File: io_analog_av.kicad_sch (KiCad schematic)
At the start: 15 parts, among them J10 ICD15S13E4GX00LF, J11 PJRAN3X1U03X, J13 SJ1-3533NG, J14 PJRAN2X1U02X, J17 K-SCARTX-022, U20 FSA2275UMX

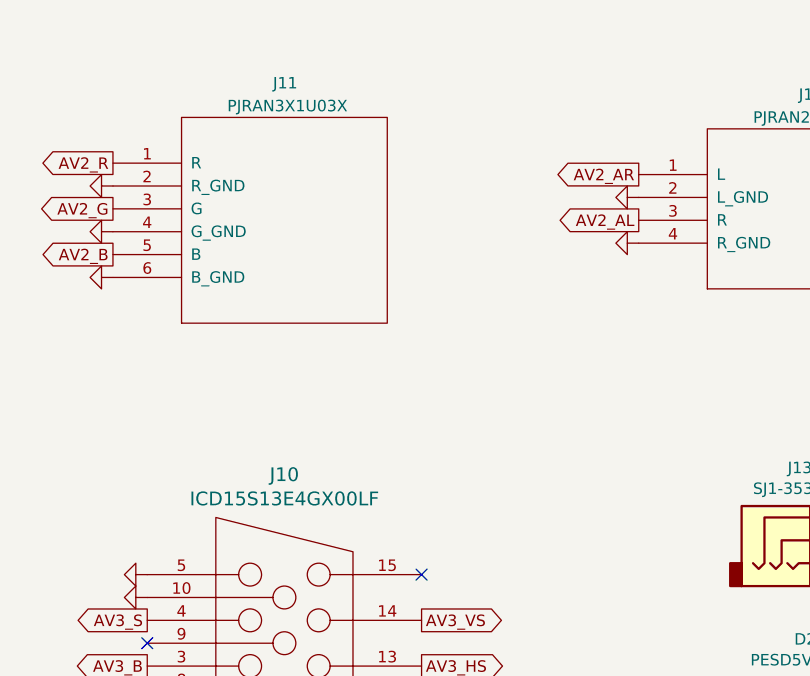
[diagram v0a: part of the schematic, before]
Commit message: update schematic to v1.5
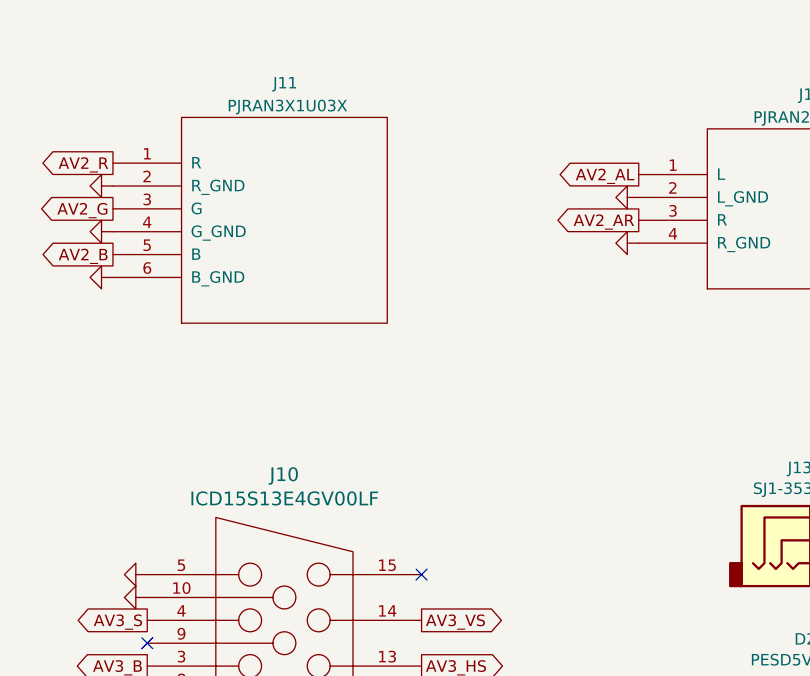
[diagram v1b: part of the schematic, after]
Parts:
- J10: value ICD15S13E4GX00LF -> ICD15S13E4GV00LF
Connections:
- net AV2_AL: now also J14.1 (L); no longer J14.3 (R)
- net AV2_AR: now also J14.3 (R); no longer J14.1 (L)

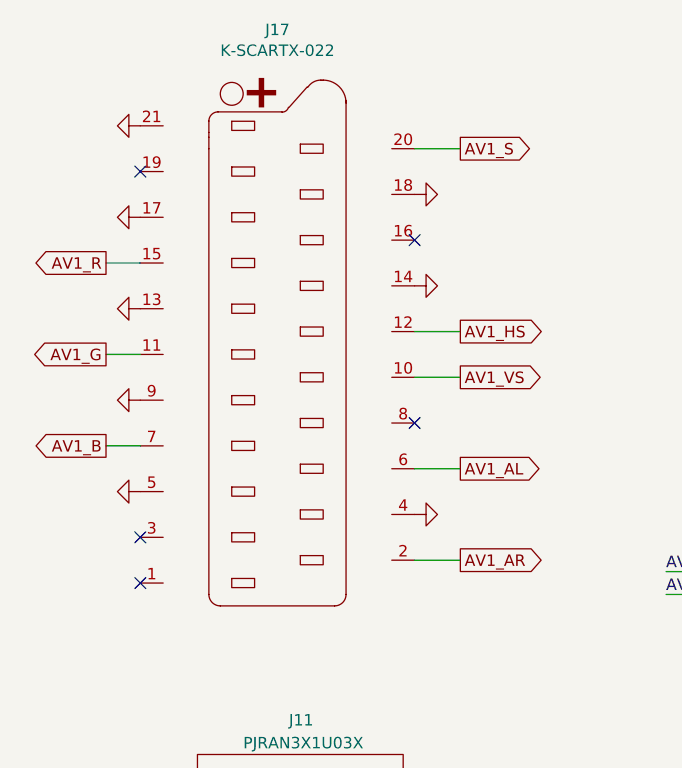
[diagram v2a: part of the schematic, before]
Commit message: fix power supply connections on v1.6 schematic
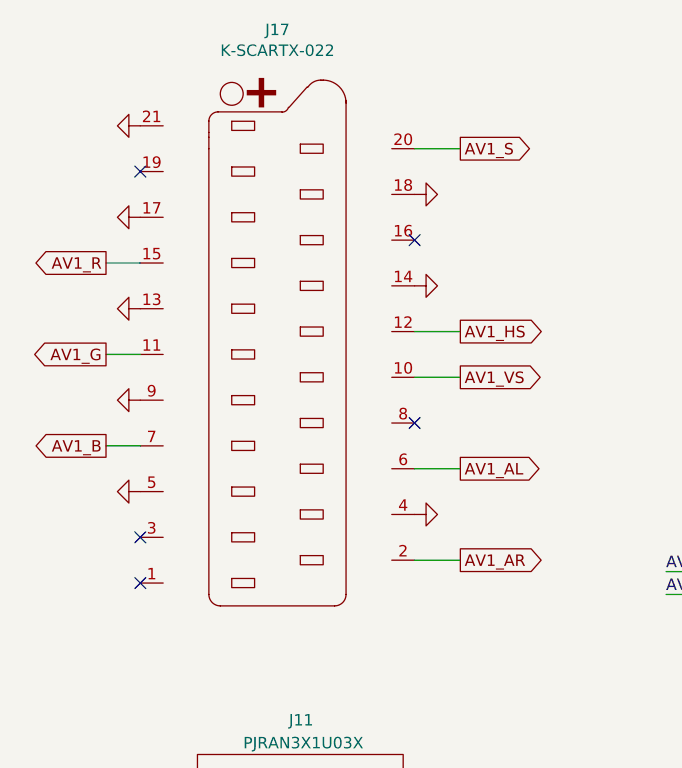
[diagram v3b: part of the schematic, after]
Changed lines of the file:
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@@
 (kicad_sch
-	(version 20231120)
+	(version 20250114)
 	(generator "eeschema")
-	(generator_version "8.0")
+	(generator_version "9.0")
 	(paper "A4")
 	(title_block
@@
 	(label "AV3_AL_MUX"
 		(at 115.57 151.13 0)
-		(fields_autoplaced yes)
 		(effects
 			(font
@@
 	(label "AV1_AR"
 		(at 97.79 68.58 0)
-		(fields_autoplaced yes)
 		(effects
 			(font
@@
 	(label "AV1_HS"
 		(at 152.4 60.96 0)
-		(fields_autoplaced yes)
 		(effects
 			(font
@@
 	(label "AV3_B"
 		(at 95.25 173.99 0)
-		(fields_autoplaced yes)
 		(effects
 			(font
@@
 	(label "AV1_R"
 		(at 97.79 36.83 0)
-		(fields_autoplaced yes)
 		(effects
 			(font
@@
 	(label "AV3_HS"
 		(at 152.4 66.04 0)
-		(fields_autoplaced yes)
 		(effects
 			(font
@@
 	(label "AV1_AL"
 		(at 97.79 66.04 0)
-		(fields_autoplaced yes)
 		(effects
 			(font
@@
 	(label "AV3_AR_MUX"
 		(at 193.04 142.24 0)
-		(fields_autoplaced yes)
 		(effects
 			(font
@@
 	(label "AV1_AL"
 		(at 232.41 132.08 0)
-		(fields_autoplaced yes)
 		(effects
 			(font
@@
 	(label "AV2_R"
 		(at 149.86 105.41 0)
-		(fields_autoplaced yes)
 		(effects
 			(font
@@
 	(label "AV3_AL_MUX"
 		(at 92.71 81.28 0)
-		(fields_autoplaced yes)
 		(effects
 			(font
@@
 	(label "AV1_B"
 		(at 97.79 44.45 0)
-		(fields_autoplaced yes)
 		(effects
 			(font
@@
 	(label "AV2_B"
 		(at 149.86 113.03 0)
-		(fields_autoplaced yes)
 		(effects
 			(font
@@
 	(label "AV1_G"
 		(at 97.79 39.37 0)
-		(fields_autoplaced yes)
 		(effects
 			(font
@@
 	(label "AV3_AR_MUX"
 		(at 92.71 83.82 0)
-		(fields_autoplaced yes)
 		(effects
 			(font
@@
 	(label "AV1_AR"
 		(at 232.41 137.16 0)
-		(fields_autoplaced yes)
 		(effects
 			(font
@@
 	(label "AV3_S"
 		(at 95.25 176.53 0)
-		(fields_autoplaced yes)
 		(effects
 			(font
@@
 	(label "AV1_S"
 		(at 97.79 46.99 0)
-		(fields_autoplaced yes)
 		(effects
 			(font
@@
 	(label "AV1_VS"
 		(at 152.4 63.5 0)
-		(fields_autoplaced yes)
 		(effects
 			(font
@@
 	(label "AV3_AR_MUX"
 		(at 115.57 148.59 0)
-		(fields_autoplaced yes)
 		(effects
 			(font
@@
 	(label "AV3_G"
 		(at 95.25 168.91 0)
-		(fields_autoplaced yes)
 		(effects
 			(font
@@
 	(label "AV2_AR"
 		(at 191.77 111.76 0)
-		(fields_autoplaced yes)
 		(effects
 			(font
@@
 	(label "AV3_VS"
 		(at 152.4 68.58 0)
-		(fields_autoplaced yes)
 		(effects
 			(font
@@
 	(label "AV2_G"
 		(at 149.86 107.95 0)
-		(fields_autoplaced yes)
 		(effects
 			(font
@@
 	(label "AV3_AL_MUX"
 		(at 193.04 139.7 0)
-		(fields_autoplaced yes)
 		(effects
 			(font
@@
 	(label "AV3_R"
 		(at 95.25 166.37 0)
-		(fields_autoplaced yes)
 		(effects
 			(font
@@
 	(label "AV2_AL"
 		(at 191.77 109.22 0)
-		(fields_autoplaced yes)
-		(effects
-			(font
+		(effects
+			(font
